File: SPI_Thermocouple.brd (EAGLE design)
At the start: 25.1 x 19 mm, 7 parts, among them U1 MAX31855

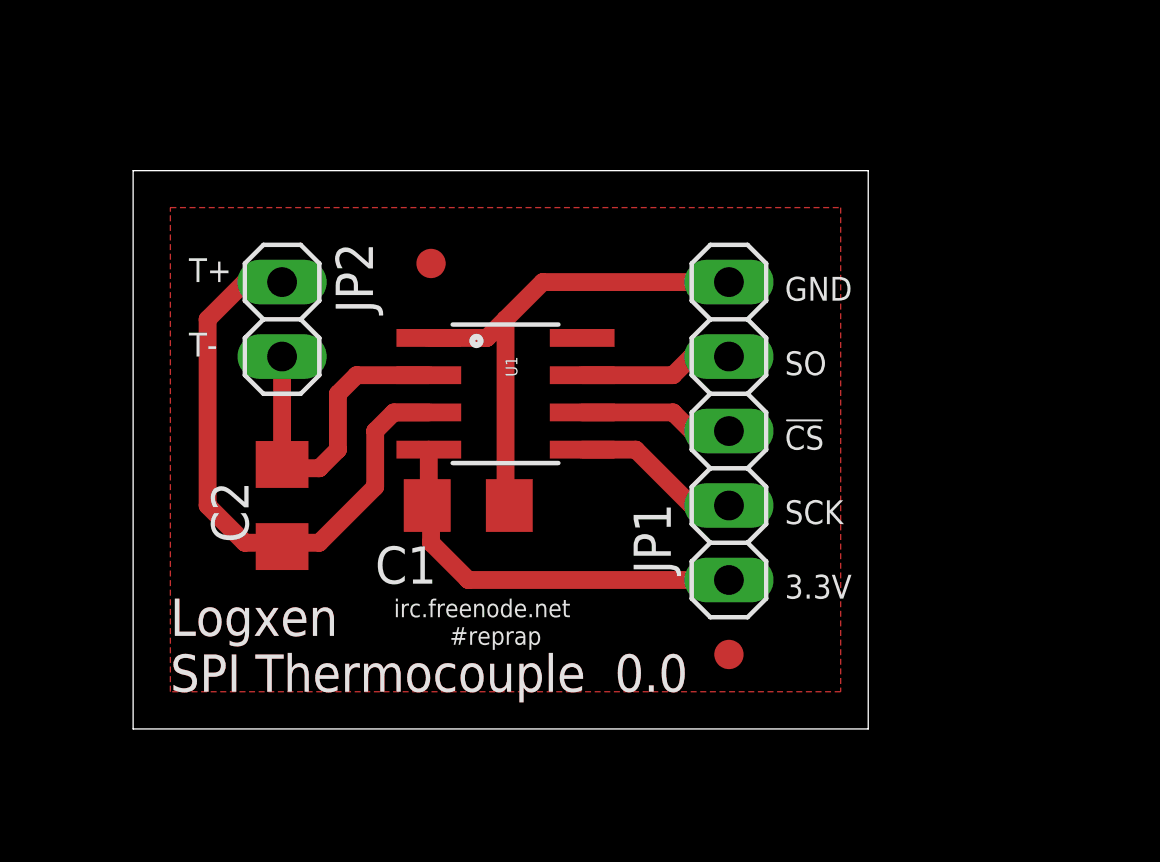
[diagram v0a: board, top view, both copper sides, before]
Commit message: straightened the traces from the thermocouple
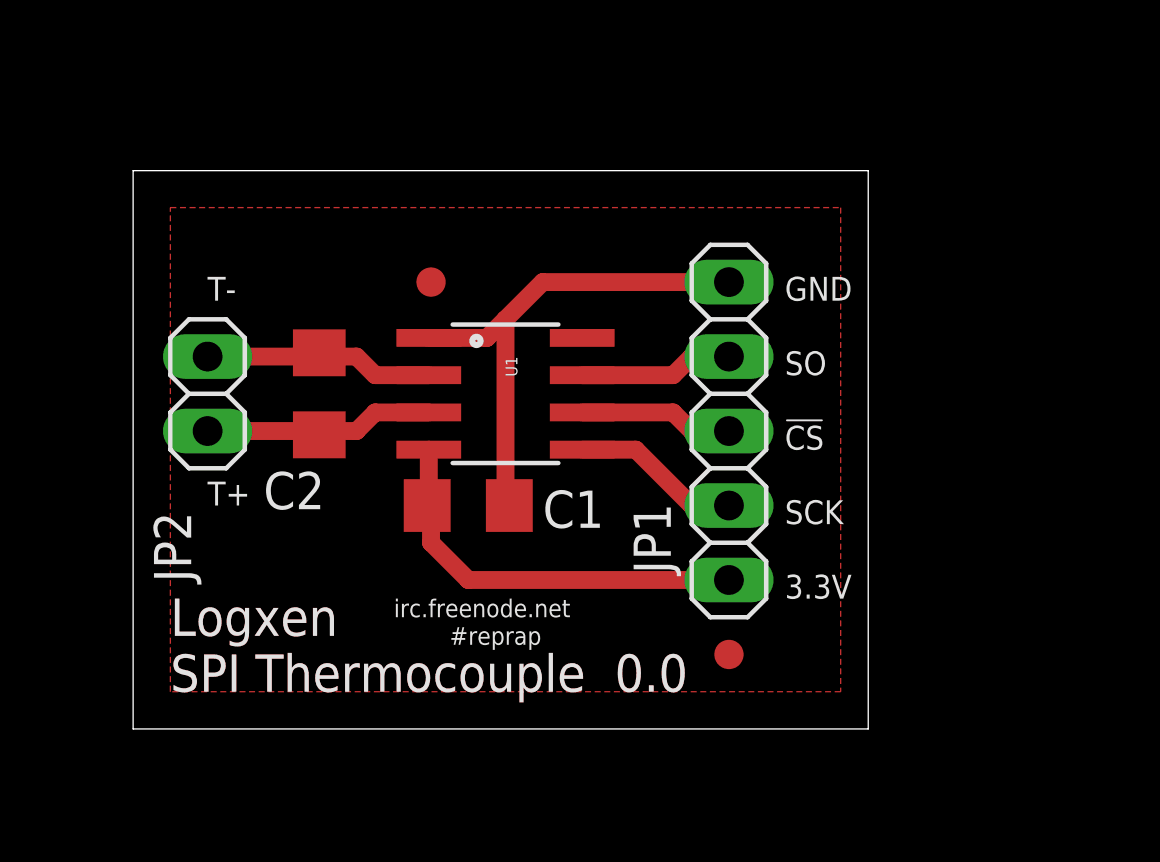
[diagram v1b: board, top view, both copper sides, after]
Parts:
- moved C2 4.02 mm to (6.35, 11.4)
- moved JP2 3.59 mm to (2.54, 11.4), turned to 90 degrees
- moved JP4 0.63 mm to (10.2, 15.2)
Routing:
- net N$1: track 20.6 -> 7.94 mm
- net N$2: track 11.2 -> 7.94 mm
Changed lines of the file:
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@@
 <text x="22.225" y="12.065" size="0.8128" layer="21">SO</text>
 <text x="22.225" y="14.605" size="0.8128" layer="21">GND</text>
-<text x="1.905" y="12.7" size="0.8128" layer="21">T-</text>
-<text x="1.905" y="15.24" size="0.8128" layer="21">T+</text>
+<text x="2.54" y="14.605" size="0.8128" layer="21">T-</text>
+<text x="2.54" y="7.62" size="0.8128" layer="21">T+</text>
 <text x="1.27" y="1.27" size="1.27" layer="21">SPI Thermocouple  0.0</text>
 <text x="8.89" y="3.81" size="0.6096" layer="21">irc.freenode.net</text>
@@
 <element name="U1" library="logxen" package="SO08" value="MAX31855" x="12.7" y="11.43" rot="R270"/>
 <element name="C1" library="resistor" package="C1206" value="0.1uF" x="11.43" y="7.62" smashed="yes">
-<attribute name="NAME" x="8.255" y="4.953" size="1.27" layer="25"/>
+<attribute name="NAME" x="13.97" y="6.858" size="1.27" layer="25"/>
 <attribute name="VALUE" x="11.43" y="5.207" size="1.27" layer="27"/>
 </element>
-<element name="C2" library="resistor" package="C1206" value="10nF" x="5.08" y="7.62" rot="R90"/>
-<element name="JP2" library="pinhead" package="1X02" value="TC" x="5.08" y="13.97" smashed="yes" rot="R270">
-<attribute name="NAME" x="6.9088" y="16.5862" size="1.27" layer="25" ratio="10" rot="R270"/>
-<attribute name="VALUE" x="3.81" y="17.145" size="1.27" layer="27"/>
+<element name="C2" library="resistor" package="C1206" value="10nF" x="6.35" y="11.43" smashed="yes" rot="R90">
+<attribute name="NAME" x="4.445" y="7.493" size="1.27" layer="25"/>
+<attribute name="VALUE" x="4.445" y="5.842" size="1.27" layer="27"/>
+</element>
+<element name="JP2" library="pinhead" package="1X02" value="TC" x="2.54" y="11.43" smashed="yes" rot="R90">
+<attribute name="NAME" x="1.9812" y="5.0038" size="1.27" layer="25" ratio="10" rot="R90"/>
+<attribute name="VALUE" x="1.27" y="15.875" size="1.27" layer="27"/>
 </element>
 <element name="JP1" library="pinhead" package="1X05" value="SPI" x="20.32" y="10.16" smashed="yes" rot="R270">
@@
 </element>
 <element name="JP3" library="SparkFun" package="FIDUCIAL-1X2" value="FIDUCIAL1X2" x="20.32" y="2.54"/>
-<element name="JP4" library="SparkFun" package="FIDUCIAL-1X2" value="FIDUCIAL1X2" x="10.16" y="15.875"/>
+<element name="JP4" library="SparkFun" package="FIDUCIAL-1X2" value="FIDUCIAL1X2" x="10.16" y="15.24"/>
 </elements>
 <signals>
@@
 <contactref element="C2" pad="1"/>
 <contactref element="JP2" pad="1"/>
-<wire x1="10.0838" y1="10.795" x2="8.89" y2="10.795" width="0.6096" layer="1"/>
-<wire x1="8.89" y1="10.795" x2="8.255" y2="10.16" width="0.6096" layer="1"/>
-<wire x1="8.255" y1="10.16" x2="8.255" y2="8.255" width="0.6096" layer="1"/>
-<wire x1="8.255" y1="8.255" x2="6.35" y2="6.35" width="0.6096" layer="1"/>
-<wire x1="6.35" y1="6.35" x2="5.08" y2="6.35" width="0.6096" layer="1"/>
-<wire x1="5.08" y1="15.24" x2="3.81" y2="15.24" width="0.6096" layer="1"/>
-<wire x1="3.81" y1="15.24" x2="2.54" y2="13.97" width="0.6096" layer="1"/>
-<wire x1="2.54" y1="13.97" x2="2.54" y2="7.62" width="0.6096" layer="1"/>
-<wire x1="2.54" y1="7.62" x2="3.81" y2="6.35" width="0.6096" layer="1"/>
-<wire x1="3.81" y1="6.35" x2="5.08" y2="6.35" width="0.6096" layer="1"/>
-<wire x1="5.08" y1="6.35" x2="5.08" y2="6.22" width="0.6096" layer="1"/>
+<wire x1="10.0838" y1="10.795" x2="8.255" y2="10.795" width="0.6096" layer="1"/>
+<wire x1="8.255" y1="10.795" x2="7.62" y2="10.16" width="0.6096" layer="1"/>
+<wire x1="7.62" y1="10.16" x2="6.35" y2="10.16" width="0.6096" layer="1"/>
+<wire x1="2.54" y1="10.16" x2="6.35" y2="10.16" width="0.6096" layer="1"/>
+<wire x1="6.35" y1="10.16" x2="6.35" y2="10.03" width="0.6096" layer="1"/>
 </signal>
 <signal name="N$2">
@@
 <contactref element="C2" pad="2"/>
 <contactref element="JP2" pad="2"/>
-<wire x1="10.0838" y1="12.065" x2="7.62" y2="12.065" width="0.6096" layer="1"/>
-<wire x1="7.62" y1="12.065" x2="6.985" y2="11.43" width="0.6096" layer="1"/>
-<wire x1="6.985" y1="11.43" x2="6.985" y2="9.525" width="0.6096" layer="1"/>
-<wire x1="6.985" y1="9.525" x2="6.35" y2="8.89" width="0.6096" layer="1"/>
-<wire x1="6.35" y1="8.89" x2="5.08" y2="8.89" width="0.6096" layer="1"/>
-<wire x1="5.08" y1="12.7" x2="5.08" y2="9.02" width="0.6096" layer="1"/>
-<wire x1="5.08" y1="8.89" x2="5.08" y2="9.02" width="0.6096" layer="1"/>
+<wire x1="10.0838" y1="12.065" x2="8.255" y2="12.065" width="0.6096" layer="1"/>
+<wire x1="8.255" y1="12.065" x2="7.62" y2="12.7" width="0.6096" layer="1"/>
+<wire x1="7.62" y1="12.7" x2="6.35" y2="12.7" width="0.6096" layer="1"/>
+<wire x1="2.54" y1="12.7" x2="6.35" y2="12.7" width="0.6096" layer="1"/>
+<wire x1="6.35" y1="12.7" x2="6.35" y2="12.83" width="0.6096" layer="1"/>
 </signal>
 <signal name="N$3">

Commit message: upgrade design to a wing
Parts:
- removed JP2: TC, pinhead:1X02
- removed JP3, JP4: FIDUCIAL1X2, SparkFun:FIDUCIAL-1X2
- added FID1, FID2, FID3: FIDUCIAL1X2, SparkFun:FIDUCIAL-1X2
- added U$1: OSHW-LOGOS, logxen:OSHW-LOGO-S
- added W1: PAPILIO-WING-8BITS, logxen:PAPILIO-WING-8BITS
- added X1: TC, con-weidmueller-sl35:180-2
- C1: device resistor:C1206 -> SparkFun-Passives:1206
- C2: device resistor:C1206 -> SparkFun-Passives:0603-CAP
- JP1: value SPI -> TC; device pinhead:1X05 -> pinhead:1X02
- moved C2 12.8 mm to (19.1, 10.2), turned to 270 degrees
- moved C1 8.52 mm to (15.2, 15.2), turned to 180 degrees
- moved JP1 2.54 mm to (22.9, 10.2)
- moved U1 1.80 mm to (14.0, 10.2), turned to 90 degrees
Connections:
- removed net N$1: C2.1, JP2.1, U1.3
- removed net N$2: C2.2, JP2.2, U1.2
- removed net N$3: JP1.3, U1.6
- removed net N$4: JP1.2, U1.7
- removed net N$5: JP1.4, U1.5
- removed net VCC: C1.1, JP1.5, U1.4
- new net 3.3V: C1.1, U1.4, W1.11
- new net 5V: W1.12
- new net MISO: U1.7, W1.7
- new net N$11: W1.4
- new net N$12: W1.3
- new net N$13: W1.2
- new net N$14: W1.1
- new net N$6: W1.8
- new net SCK: U1.5, W1.6
- new net SSEL: U1.6, W1.5
- new net T+: C2.1, JP1.1, U1.3, X1.1
- new net T-: C2.2, JP1.2, U1.2, X1.2
- net GND: now also W1.9; no longer JP1.1
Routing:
- net 3.3V: track 0.00 -> 21.5 mm, vias 0 -> 1
- net MISO: track 0.00 -> 18.8 mm, vias 0 -> 1
- net GND: track 17.5 -> 0.00 mm
- net VCC: track 14.0 -> 0.00 mm
- net SCK: track 0.00 -> 13.2 mm, vias 0 -> 1
- net T+: track 0.00 -> 12.3 mm
- net T-: track 0.00 -> 12.3 mm
- net SSEL: track 0.00 -> 10.9 mm, vias 0 -> 1
- net N$2: track 7.94 -> 0.00 mm
- net N$1: track 7.94 -> 0.00 mm
- net N$5: track 5.79 -> 0.00 mm
- net N$4: track 5.27 -> 0.00 mm
- net N$3: track 5.27 -> 0.00 mm
- added copper zone on layer 16, net GND
- added copper zone on layer 1, net N$1
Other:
- board size 25.1 x 19 mm -> 29.2 x 20.3 mm
- board text added: "Proto1"
- board text added: "SPI Thermocouple"
- board text added: "design by Logxen"
- board text removed: "#reprap"
- board text removed: "Logxen"
- board text removed: "SPI Thermocouple 0.0"
- board text removed: "irc.freenode.net"
